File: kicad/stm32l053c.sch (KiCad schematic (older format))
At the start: 55 parts, among them J1 Water_Level, J2 Motion, J3 Door, J4 Door_Led, J6 Pump, J7 BATTERY, P1 SWD, Q1 Q_NMOS_GSD, Q2 Q_PMOS_GSD, U1 MCP1703A-5002_SOT223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

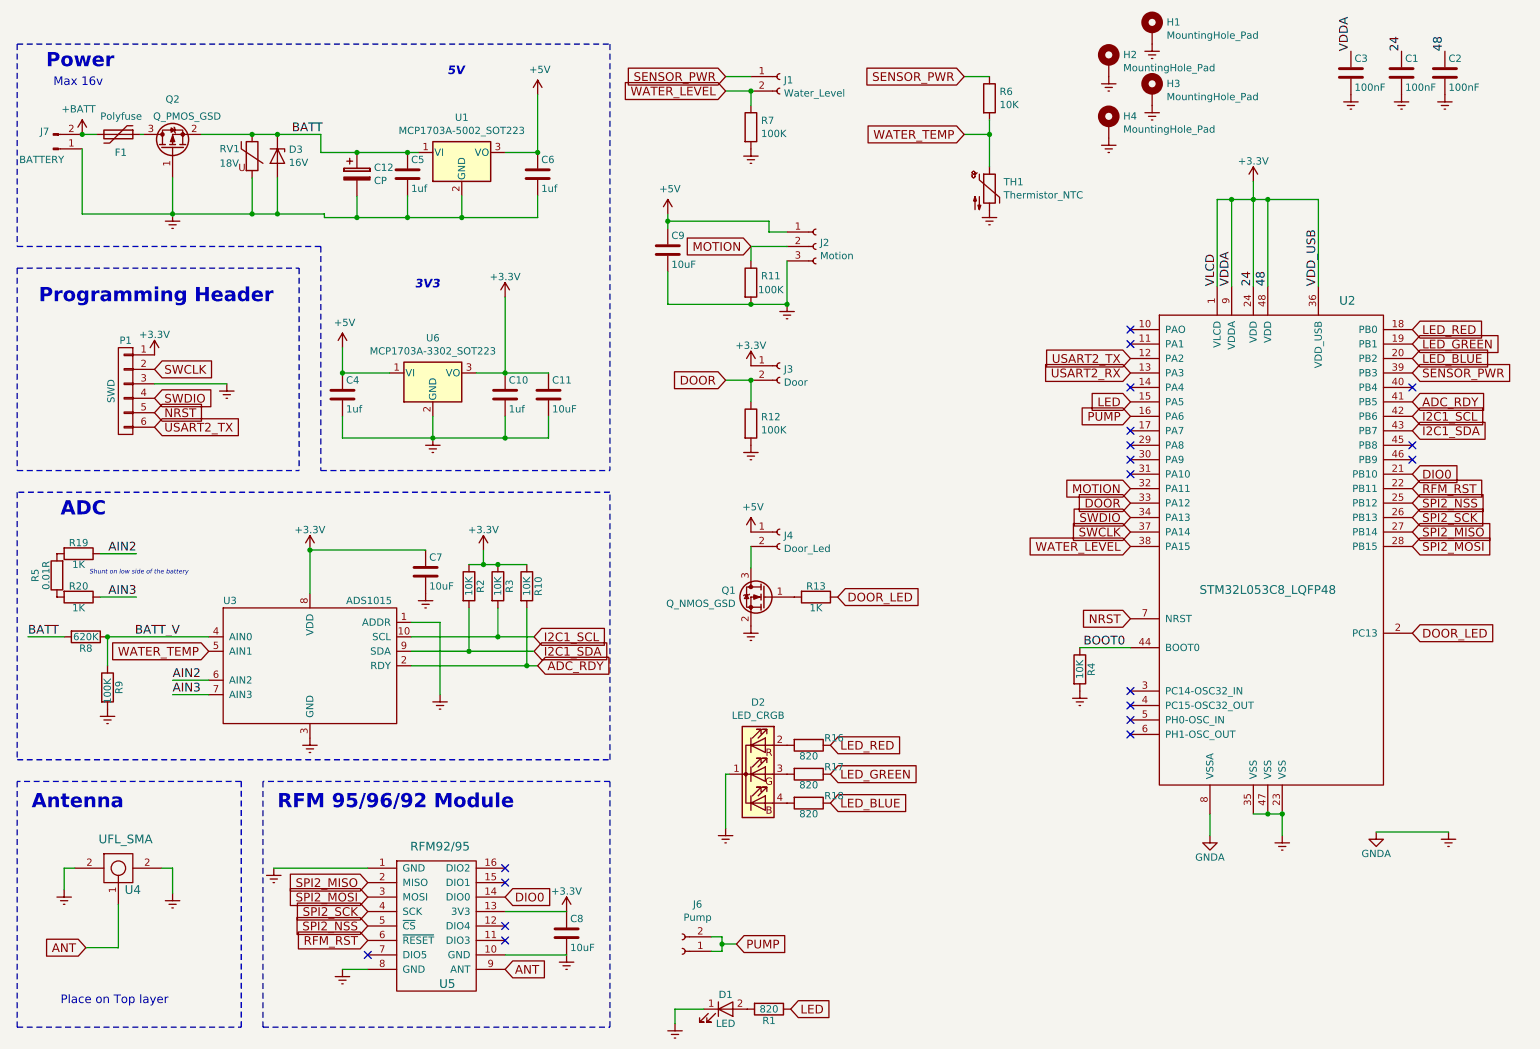
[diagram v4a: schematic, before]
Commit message: Power switch
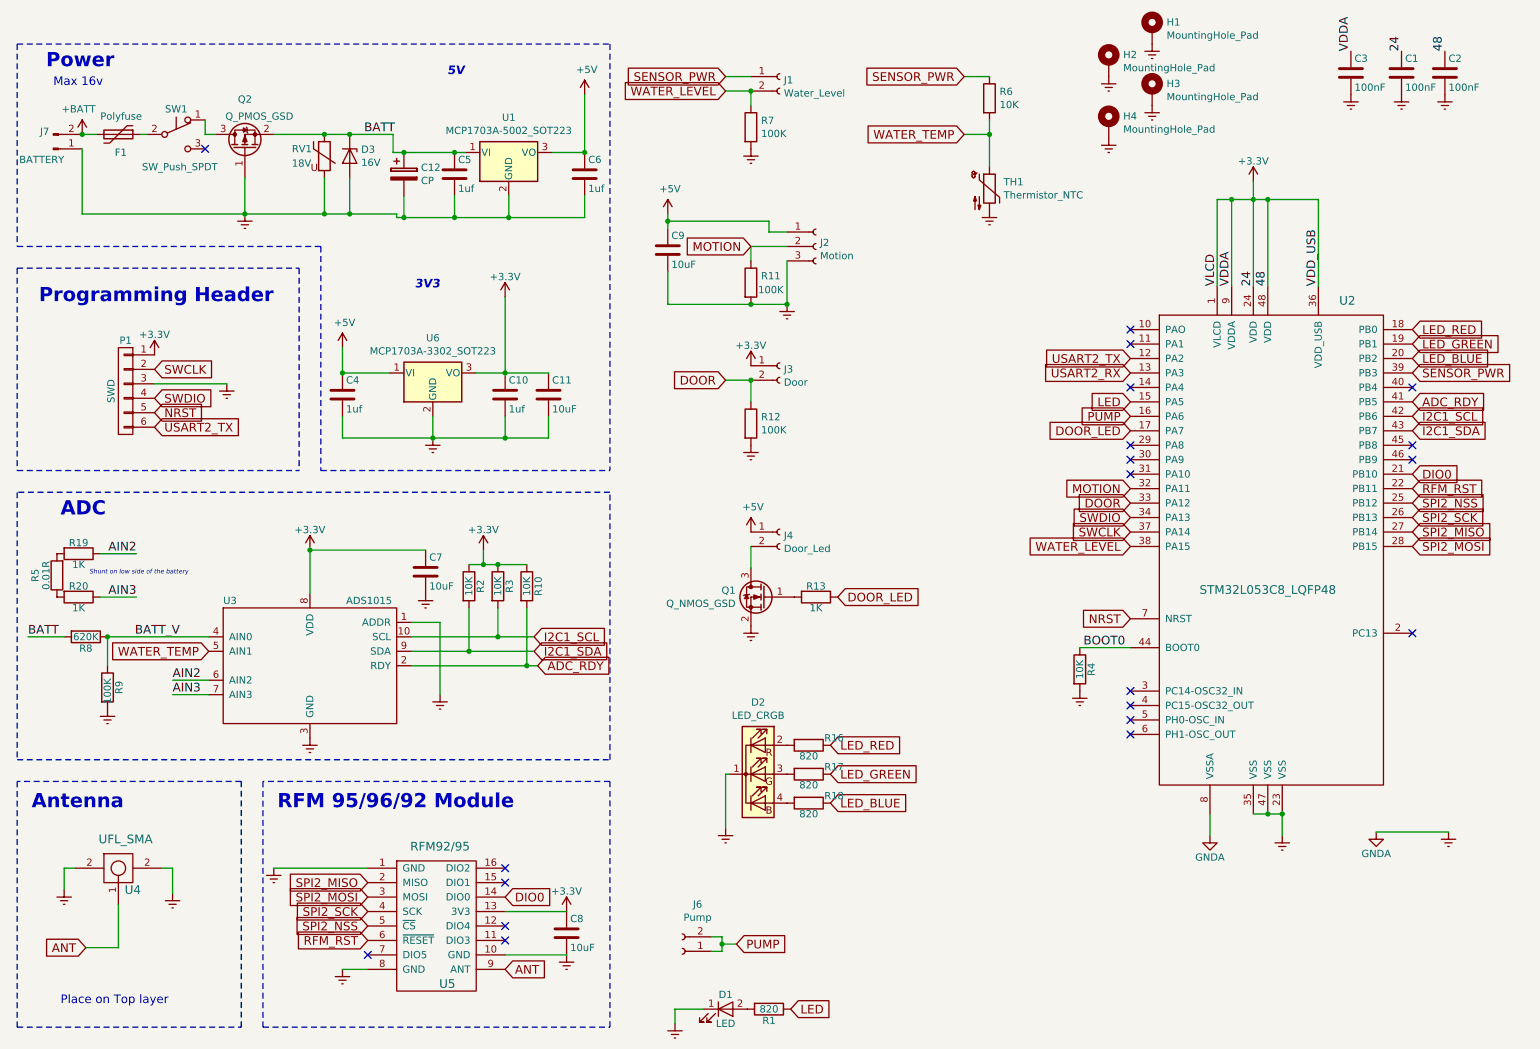
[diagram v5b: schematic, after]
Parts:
- added SW1: SW_Push_SPDT, Connector_PinHeader_2.54mm:PinHeader_1x03_P2.54mm_Vertical, symbol Switch:SW_Push_SPDT
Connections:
- net DOOR_LED: now also U2.17 (PA7); no longer U2.2 (PC13)
- net at Q2.3 (D): now also SW1.1 (A); no longer F1.1
- new net: F1.1, SW1.2 (B)
- no-connect marks 19 -> 20
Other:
- moved on the sheet: C12, C5, C6, D3, Q2, RV1, U1
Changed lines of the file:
@@
 L stm32l053c-rescue:C C5
 U 1 1 59302470
-P 3675 1625
-F 0 "C5" H 3700 1725 50  0000 L CNN
-F 1 "1uf" H 3700 1525 50  0000 L CNN
-F 2 "Capacitor_SMD:C_0805_2012Metric_Pad1.15x1.40mm_HandSolder" H 3713 1475 50  0001 C CNN
-F 3 "" H 3675 1625 50  0001 C CNN
-	1    3675 1625
+P 4000 1625
+F 0 "C5" H 4025 1725 50  0000 L CNN
+F 1 "1uf" H 4025 1525 50  0000 L CNN
+F 2 "Capacitor_SMD:C_0805_2012Metric_Pad1.15x1.40mm_HandSolder" H 4038 1475 50  0001 C CNN
+F 3 "" H 4000 1625 50  0001 C CNN
+	1    4000 1625
 	1    0    0    -1
 $EndComp
@@
 L stm32l053c-rescue:C C6
 U 1 1 5930294B
-P 4575 1625
-F 0 "C6" H 4600 1725 50  0000 L CNN
-F 1 "1uf" H 4600 1525 50  0000 L CNN
-F 2 "Capacitor_SMD:C_0805_2012Metric_Pad1.15x1.40mm_HandSolder" H 4613 1475 50  0001 C CNN
-F 3 "" H 4575 1625 50  0001 C CNN
-	1    4575 1625
+P 4900 1625
+F 0 "C6" H 4925 1725 50  0000 L CNN
+F 1 "1uf" H 4925 1525 50  0000 L CNN
+F 2 "Capacitor_SMD:C_0805_2012Metric_Pad1.15x1.40mm_HandSolder" H 4938 1475 50  0001 C CNN
+F 3 "" H 4900 1625 50  0001 C CNN
+	1    4900 1625
 	1    0    0    -1
 $EndComp
@@
 	3700 5025 4500 5025
 Wire Wire Line
-	3675 1925 3675 1775
-Wire Wire Line
-	4575 1925 4575 1775
-Connection ~ 4050 1925
+	4000 1925 4000 1775
+Wire Wire Line
+	4900 1925 4900 1775
+Connection ~ 4375 1925
 Wire Wire Line
 	3000 4225 3800 4225
@@
 	1    0    0    -1
 $EndComp
-Connection ~ 4575 1475
+Connection ~ 4900 1475
 $Comp
 L stm32l053c-rescue:R R10
@@
 Connection ~ 4500 5025
 Connection ~ 4300 4325
-Text Label 2875 1350 0    60   ~ 0
+Text Label 3375 1350 0    60   ~ 0
 BATT
 Wire Wire Line
@@
 USART2_RX
 Wire Wire Line
-	4050 1775 4050 1925
+	4375 1775 4375 1925
 Connection ~ 9725 6050
 $Comp
@@
 Wire Wire Line
 	5875 950  6050 950
-Text GLabel 10625 4800 2    60   Input ~ 0
+Text GLabel 8675 3400 0    60   Input ~ 0
 DOOR_LED
 $Comp
@@
 NoConn ~ 10625 3100
 NoConn ~ 10625 3600
-NoConn ~ 8675 3400
 NoConn ~ 8675 3500
 NoConn ~ 8675 3600
@@
 L Regulator_Linear:MCP1703A-5002_SOT223 U1
 U 1 1 5C257B3B
-P 4050 1475
-F 0 "U1" H 4050 1717 50  0000 C CNN
-F 1 "MCP1703A-5002_SOT223" H 4050 1626 50  0000 C CNN
-F 2 "Package_TO_SOT_SMD:SOT-223-3_TabPin2" H 4050 1675 50  0001 C CNN
-F 3 "http://ww1.microchip.com/downloads/en/DeviceDoc/20005122B.pdf" H 4050 1425 50  0001 C CNN
-	1    4050 1475
+P 4375 1475
+F 0 "U1" H 4375 1717 50  0000 C CNN
+F 1 "MCP1703A-5002_SOT223" H 4375 1626 50  0000 C CNN
+F 2 "Package_TO_SOT_SMD:SOT-223-3_TabPin2" H 4375 1675 50  0001 C CNN
+F 3 "http://ww1.microchip.com/downloads/en/DeviceDoc/20005122B.pdf" H 4375 1425 50  0001 C CNN
+	1    4375 1475
 	1    0    0    -1
 $EndComp
@@
 L power:+5V #PWR028
 U 1 1 5C257EAB
-P 4575 1075
-F 0 "#PWR028" H 4575 925 50  0001 C CNN
-F 1 "+5V" H 4590 1248 50  0000 C CNN
-F 2 "" H 4575 1075 50  0001 C CNN
-F 3 "" H 4575 1075 50  0001 C CNN
-	1    4575 1075
+P 4900 1075
+F 0 "#PWR028" H 4900 925 50  0001 C CNN
+F 1 "+5V" H 4915 1248 50  0000 C CNN
+F 2 "" H 4900 1075 50  0001 C CNN
+F 3 "" H 4900 1075 50  0001 C CNN
+	1    4900 1075
 	1    0    0    -1
 $EndComp
@@
 L Device:CP C12
 U 1 1 5C265527
-P 3325 1625
-F 0 "C12" H 3443 1671 50  0000 L CNN
-F 1 "CP" H 3443 1580 50  0000 L CNN
-F 2 "Capacitor_THT:CP_Radial_D8.0mm_P3.50mm" H 3363 1475 50  0001 C CNN
-F 3 "~" H 3325 1625 50  0001 C CNN
-	1    3325 1625
-	1    0    0    -1
-$EndComp
-Wire Wire Line
-	3675 1475 3325 1475
-Wire Wire Line
-	3325 1775 3325 1925
-Wire Wire Line
-	3325 1925 3675 1925
+P 3650 1625
+F 0 "C12" H 3768 1671 50  0000 L CNN
+F 1 "CP" H 3768 1580 50  0000 L CNN
+F 2 "Capacitor_THT:CP_Radial_D8.0mm_P3.50mm" H 3688 1475 50  0001 C CNN
+F 3 "~" H 3650 1625 50  0001 C CNN
+	1    3650 1625
+	1    0    0    -1
+$EndComp
+Wire Wire Line
+	4000 1475 3650 1475
+Wire Wire Line
+	3650 1775 3650 1925
+Wire Wire Line
+	3650 1925 4000 1925
 $Comp
 L Connector:Conn_01x02_Female J6
@@
 L Device:Q_PMOS_GSD Q2
 U 1 1 5C293199
-P 2050 1450
-F 0 "Q2" V 2393 1450 50  0000 C CNN
-F 1 "Q_PMOS_GSD" V 2275 1350 50  0000 C CNN
-F 2 "Package_TO_SOT_SMD:SOT-23_Handsoldering" H 2250 1550 50  0001 C CNN
-F 3 "~" H 2050 1450 50  0001 C CNN
-	1    2050 1450
+P 2550 1450
+F 0 "Q2" V 2893 1450 50  0000 C CNN
+F 1 "Q_PMOS_GSD" V 2775 1350 50  0000 C CNN
+F 2 "Package_TO_SOT_SMD:SOT-23_Handsoldering" H 2750 1550 50  0001 C CNN
+F 3 "~" H 2550 1450 50  0001 C CNN
+	1    2550 1450
 	0    -1   -1   0
 $EndComp
-Connection ~ 1425 1350
-Wire Wire Line
-	1425 1350 1525 1350
-Wire Wire Line
-	2250 1350 2600 1350
+Wire Wire Line
+	2750 1350 3100 1350
 $Comp
 L power:Earth #PWR045
 U 1 1 5C2A4DC2
-P 2050 1900
-F 0 "#PWR045" H 2050 1650 50  0001 C CNN
-F 1 "Earth" H 2050 1750 50  0001 C CNN
-F 2 "" H 2050 1900 50  0000 C CNN
-F 3 "" H 2050 1900 50  0000 C CNN
-	1    2050 1900
+P 2550 1900
+F 0 "#PWR045" H 2550 1650 50  0001 C CNN
+F 1 "Earth" H 2550 1750 50  0001 C CNN
+F 2 "" H 2550 1900 50  0000 C CNN
+F 3 "" H 2550 1900 50  0000 C CNN
+	1    2550 1900
 	-1   0    0    -1
 $EndComp
 Wire Wire Line
-	4050 1925 4575 1925
-Wire Wire Line
-	4350 1475 4575 1475
+	4375 1925 4900 1925
+Wire Wire Line
+	4675 1475 4900 1475
 $Comp
 L Device:Polyfuse F1
@@
 	0    1    1    0
 $EndComp
-Connection ~ 3325 1475
+Connection ~ 3650 1475
 Wire Wire Line
 	4150 3000 4350 3000
@@
 	4350 3000 4350 2475
 Wire Wire Line
-	4575 1475 4575 1075
-Wire Wire Line
-	3750 1475 3675 1475
-Connection ~ 3675 1475
-Wire Wire Line
-	3675 1925 4050 1925
-Connection ~ 3675 1925
+	4900 1475 4900 1075
+Wire Wire Line
+	4075 1475 4000 1475
+Connection ~ 4000 1475
+Wire Wire Line
+	4000 1925 4375 1925
+Connection ~ 4000 1925
 NoConn ~ 8675 2700
 Wire Wire Line
-	3075 1475 3325 1475
-Wire Wire Line
-	1825 1350 1850 1350
+	3575 1475 3650 1475
 $Comp
 L Device:D_Zener D3
 U 1 1 5C279215
-P 2775 1500
-F 0 "D3" V 2729 1579 50  0000 L CNN
-F 1 "16V" V 2820 1579 50  0000 L CNN
-F 2 "Diode_THT:D_T-1_P5.08mm_Horizontal" H 2775 1500 50  0001 C CNN
-F 3 "~" H 2775 1500 50  0001 C CNN
-	1    2775 1500
+P 3275 1500
+F 0 "D3" V 3229 1579 50  0000 L CNN
+F 1 "16V" V 3320 1579 50  0000 L CNN
+F 2 "Diode_THT:D_T-1_P5.08mm_Horizontal" H 3275 1500 50  0001 C CNN
+F 3 "~" H 3275 1500 50  0001 C CNN
+	1    3275 1500
 	0    1    1    0
 $EndComp
@@
 L Device:Varistor RV1
 U 1 1 5C2A57EF
-P 2600 1500
-F 0 "RV1" H 2375 1550 50  0000 L CNN
-F 1 "18V" H 2375 1450 50  0000 L CNN
-F 2 "Varistor:RV_Disc_D7mm_W5.4mm_P5mm" V 2530 1500 50  0001 C CNN
-F 3 "~" H 2600 1500 50  0001 C CNN
-	1    2600 1500
-	1    0    0    -1
-$EndComp
-Connection ~ 2600 1350
-Wire Wire Line
-	2600 1350 2775 1350
-Connection ~ 2775 1350
-Wire Wire Line
-	3075 1350 3075 1475
-Wire Wire Line
-	2775 1350 3075 1350
+P 3100 1500
+F 0 "RV1" H 2875 1550 50  0000 L CNN
+F 1 "18V" H 2875 1450 50  0000 L CNN
+F 2 "Varistor:RV_Disc_D7mm_W5.4mm_P5mm" V 3030 1500 50  0001 C CNN
+F 3 "~" H 3100 1500 50  0001 C CNN
+	1    3100 1500
+	1    0    0    -1
+$EndComp
+Connection ~ 3100 1350
+Wire Wire Line
+	3100 1350 3275 1350
+Connection ~ 3275 1350
+Wire Wire Line
+	3575 1350 3575 1475
+Wire Wire Line
+	3275 1350 3575 1350
 Wire Wire Line
 	5475 2300 5475 2525
@@
 	5475 1950 5475 2000
 Wire Wire Line
-	2050 1650 2050 1900
-Wire Wire Line
-	2600 1650 2600 1900
-Wire Wire Line
-	2600 1900 2050 1900
-Connection ~ 2050 1900
-Wire Wire Line
-	2775 1650 2775 1900
-Wire Wire Line
-	2775 1900 2600 1900
-Connection ~ 2600 1900
+	2550 1650 2550 1900
+Wire Wire Line
+	3100 1650 3100 1900
+Wire Wire Line
+	3100 1900 2550 1900
+Connection ~ 2550 1900
+Wire Wire Line
+	3275 1650 3275 1900
+Wire Wire Line
+	3275 1900 3100 1900
+Connection ~ 3100 1900
 Wire Wire Line
 	1425 1450 1425 1900
 Wire Wire Line
-	1425 1900 2050 1900
-Wire Wire Line
-	2775 1900 3100 1900
-Wire Wire Line
-	3100 1900 3100 1925
-Wire Wire Line
-	3100 1925 3325 1925
-Connection ~ 2775 1900
-Connection ~ 3325 1925
+	1425 1900 2550 1900
+Wire Wire Line
+	3275 1900 3600 1900
+Wire Wire Line
+	3600 1900 3600 1925
+Wire Wire Line
+	3600 1925 3650 1925
+Connection ~ 3275 1900
+Connection ~ 3650 1925
 Text Label 1800 4250 2    60   ~ 0
 AIN2
@@
 	1600 4825 2300 4825
 Connection ~ 1600 4825
+$Comp
+L Switch:SW_Push_SPDT SW1
+U 1 1 5C27AD7E
+P 2075 1350
+F 0 "SW1" H 2075 1525 50  0000 C CNN
+F 1 "SW_Push_SPDT" H 2100 1125 50  0000 C CNN
+F 2 "Connector_PinHeader_2.54mm:PinHeader_1x03_P2.54mm_Vertical" H 2075 1350 50  0001 C CNN
+F 3 "" H 2075 1350 50  0001 C CNN
+	1    2075 1350
+	1    0    0    -1
+$EndComp
+Wire Wire Line
+	1525 1350 1425 1350
+Connection ~ 1425 1350
+NoConn ~ 2275 1450
+NoConn ~ 10625 4800
+Wire Wire Line
+	1825 1350 1875 1350
+Wire Wire Line
+	2275 1250 2275 1350
+Wire Wire Line
+	2275 1350 2350 1350
 $EndSCHEMATC
